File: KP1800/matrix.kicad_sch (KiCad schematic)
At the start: 216 parts

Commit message: Formatted Matrix
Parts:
- removed D103, D104, D105, D106, D107, D108, D18, D36, D72, D90: Diode, symbol ScottoKeebs:Placeholder_Diode
- removed S103, S104, S105, S106, S107, S108, S18, S36, S72, S90: Keyswitch, symbol ScottoKeebs:Placeholder_Keyswitch
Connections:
- net A14: now also S54.1
- net A15: now also S35.1, S53.1, S71.1, S89.1
- net B0: now also S19.1, S37.1, S55.1, S73.1, S91.1
- net B1: now also S20.1, S38.1, S56.1, S74.1, S92.1
- net B10: now also S101.1, S29.1, S47.1, S65.1, S83.1
- net B11: now also S102.1, S30.1, S48.1, S66.1, S84.1
- net B12: now also S31.1, S49.1, S67.1, S85.1
- net B13: now also S32.1, S50.1, S68.1, S86.1
- net B14: now also S33.1, S51.1, S69.1, S87.1
- net B15: now also S34.1, S52.1, S70.1, S88.1
- net B2: now also S21.1, S39.1, S57.1, S75.1, S93.1
- net B3: now also S22.1, S40.1, S58.1, S76.1, S94.1
- net B4: now also S23.1, S41.1, S59.1, S77.1, S95.1
- net B5: now also S24.1, S42.1, S60.1, S78.1, S96.1
- net B6: now also S25.1, S43.1, S61.1, S79.1, S97.1
- net B7: now also S26.1, S44.1, S62.1, S80.1, S98.1
- net B8: now also S27.1, S45.1, S63.1, S81.1, S99.1
- net B9: now also S100.1, S28.1, S46.1, S64.1, S82.1
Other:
- title: (none) -> KP1800 Matrix
- moved on the sheet: D1, D10, D100, D101, D102, D11, D12, D13, D14, D15, D16, D17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

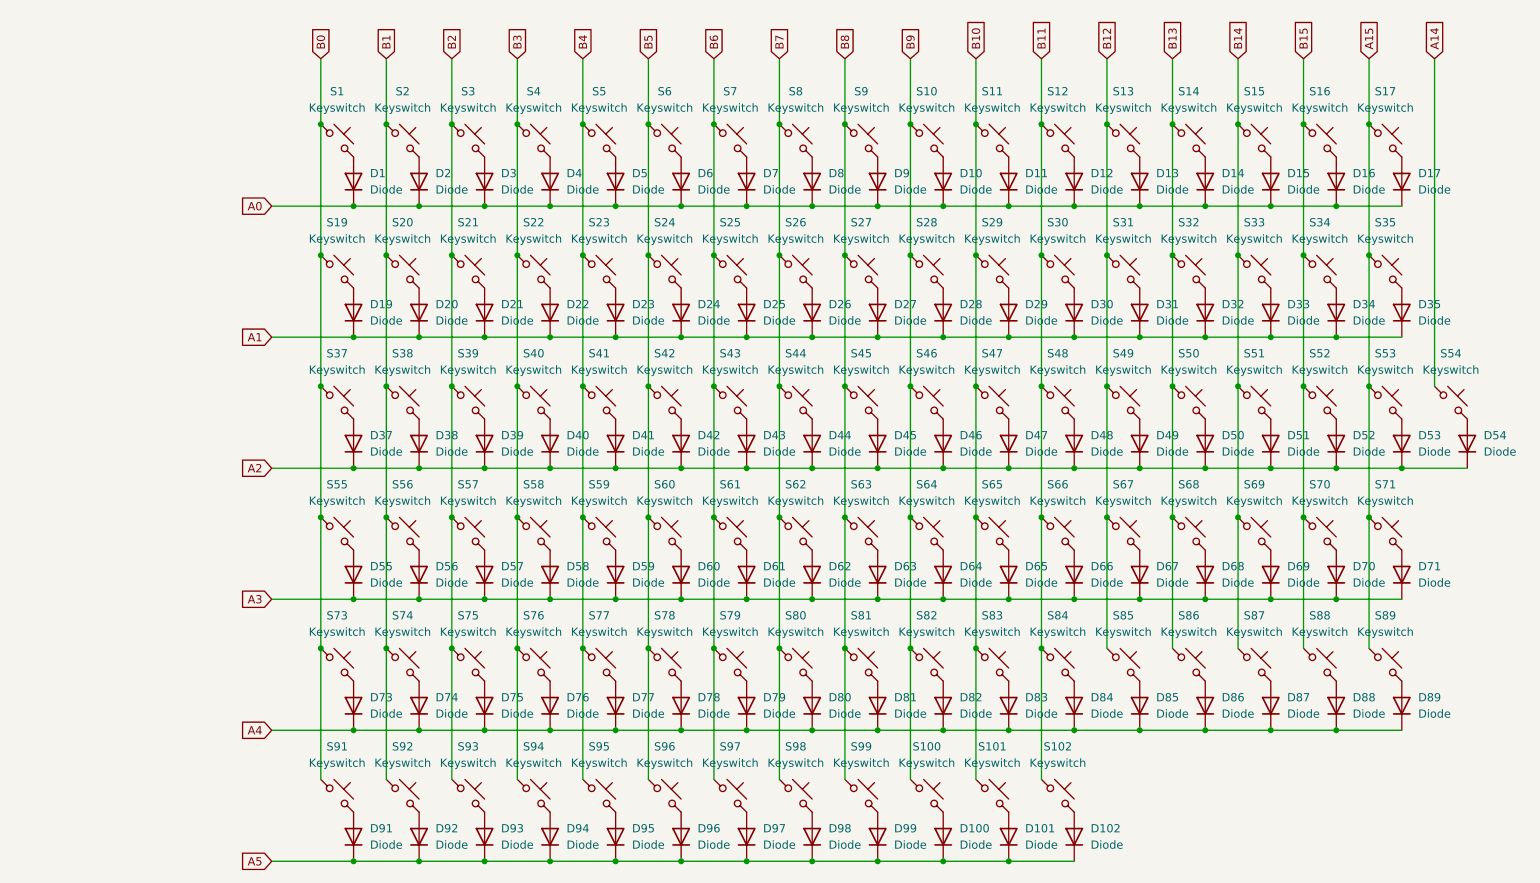
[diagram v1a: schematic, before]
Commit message: Working on PCB // Laid out key switches // 60% board
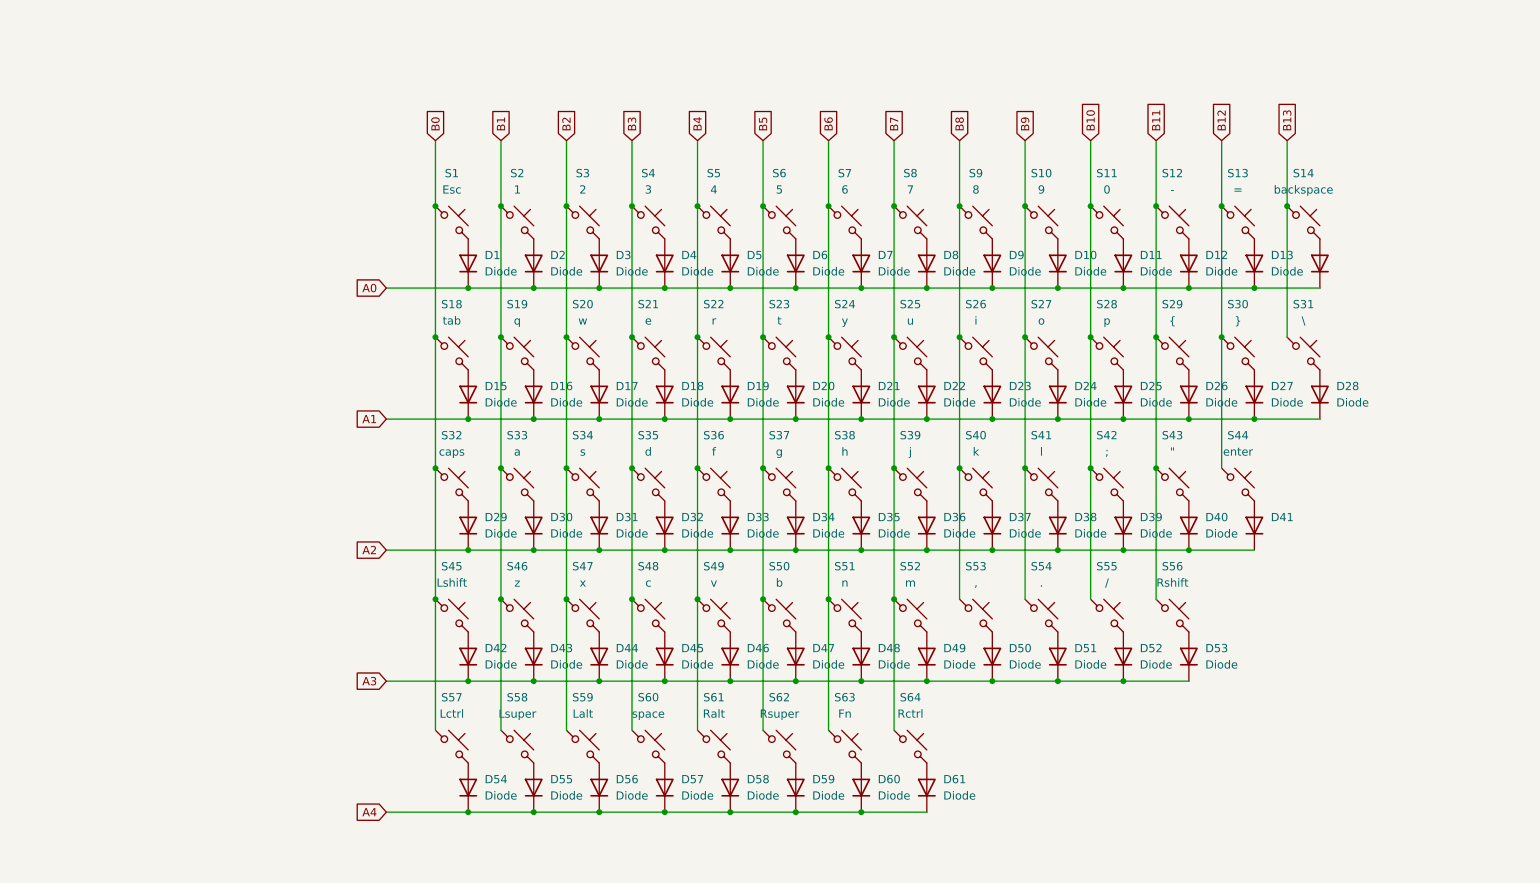
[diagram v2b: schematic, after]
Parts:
- removed D100, D101, D102, D62, D63, D64, D65, D66, D67, D68, D69, D70, D71, D73, D74, D75, D76, D77, D78, D79, D80, D81, D82, D83, D84, D85, D86, D87, D88, D89, D91, D92, D93, D94, D95, D96, D97, D98, D99: Diode, symbol ScottoKeebs:Placeholder_Diode
- removed S100, S101, S102, S15, S16, S17, S65, S66, S67, S68, S69, S70, S71, S73, S74, S75, S76, S77, S78, S79, S80, S81, S82, S83, S84, S85, S86, S87, S88, S89, S91, S92, S93, S94, S95, S96, S97, S98, S99: Keyswitch, symbol ScottoKeebs:Placeholder_Keyswitch
- added D18, D36: Diode, Diode_SMD:D_SOD-123, symbol ScottoKeebs:Placeholder_Diode
- added S18: tab, ScottoKeebs_MX:MX_PCB_1.50u, symbol ScottoKeebs:Placeholder_Keyswitch
- added S36: f, ScottoKeebs_MX:MX_PCB_1.00u, symbol ScottoKeebs:Placeholder_Keyswitch
- D1, D10, D11, D12, D13, D14, D15, D16, D17, D19, D2, D20, D21, D22, D23, D24, D25, D26, D27, D28, D29, D3, D30, D31, D32, D33, D34, D35, D37, D38, D39, D4, D40, D41, D42, D43, D44, D45, D46, D47, D48, D49, D5, D50, D51, D52, D53, D54, D55, D56, D57, D58, D59, D6, D60, D61, D7, D8, D9: footprint (none) -> Diode_SMD:D_SOD-123
- S1: value Keyswitch -> Esc; footprint (none) -> ScottoKeebs_MX:MX_PCB_1.00u
- S10: value Keyswitch -> 9; footprint (none) -> ScottoKeebs_MX:MX_PCB_1.00u
- S11: value Keyswitch -> 0; footprint (none) -> ScottoKeebs_MX:MX_PCB_1.00u
- S12: value Keyswitch -> -; footprint (none) -> ScottoKeebs_MX:MX_PCB_1.00u
- S13: value Keyswitch -> =; footprint (none) -> ScottoKeebs_MX:MX_PCB_1.00u
- S14: value Keyswitch -> backspace; footprint (none) -> ScottoKeebs_MX:MX_PCB_2.00u
- S19: value Keyswitch -> q; footprint (none) -> ScottoKeebs_MX:MX_PCB_1.00u
- S2: value Keyswitch -> 1; footprint (none) -> ScottoKeebs_MX:MX_PCB_1.00u
- S20: value Keyswitch -> w; footprint (none) -> ScottoKeebs_MX:MX_PCB_1.00u
- S21: value Keyswitch -> e; footprint (none) -> ScottoKeebs_MX:MX_PCB_1.00u
- S22: value Keyswitch -> r; footprint (none) -> ScottoKeebs_MX:MX_PCB_1.00u
- S23: value Keyswitch -> t; footprint (none) -> ScottoKeebs_MX:MX_PCB_1.00u
- S24: value Keyswitch -> y; footprint (none) -> ScottoKeebs_MX:MX_PCB_1.00u
- S25: value Keyswitch -> u; footprint (none) -> ScottoKeebs_MX:MX_PCB_1.00u
- S26: value Keyswitch -> i; footprint (none) -> ScottoKeebs_MX:MX_PCB_1.00u
- S27: value Keyswitch -> o; footprint (none) -> ScottoKeebs_MX:MX_PCB_1.00u
- S28: value Keyswitch -> p; footprint (none) -> ScottoKeebs_MX:MX_PCB_1.00u
- S29: value Keyswitch -> {; footprint (none) -> ScottoKeebs_MX:MX_PCB_1.00u
- S3: value Keyswitch -> 2; footprint (none) -> ScottoKeebs_MX:MX_PCB_1.00u
- S30: value Keyswitch -> }; footprint (none) -> ScottoKeebs_MX:MX_PCB_1.00u
- S31: value Keyswitch -> \; footprint (none) -> ScottoKeebs_MX:MX_PCB_1.50u
- S32: value Keyswitch -> caps; footprint (none) -> ScottoKeebs_MX:MX_PCB_1.75u
- S33: value Keyswitch -> a; footprint (none) -> ScottoKeebs_MX:MX_PCB_1.00u
- S34: value Keyswitch -> s; footprint (none) -> ScottoKeebs_MX:MX_PCB_1.00u
- S35: value Keyswitch -> d; footprint (none) -> ScottoKeebs_MX:MX_PCB_1.00u
- S37: value Keyswitch -> g; footprint (none) -> ScottoKeebs_MX:MX_PCB_1.00u
- S38: value Keyswitch -> h; footprint (none) -> ScottoKeebs_MX:MX_PCB_1.00u
- S39: value Keyswitch -> j; footprint (none) -> ScottoKeebs_MX:MX_PCB_1.00u
- S4: value Keyswitch -> 3; footprint (none) -> ScottoKeebs_MX:MX_PCB_1.00u
- S40: value Keyswitch -> k; footprint (none) -> ScottoKeebs_MX:MX_PCB_1.00u
- S41: value Keyswitch -> l; footprint (none) -> ScottoKeebs_MX:MX_PCB_1.00u
- S42: value Keyswitch -> ;; footprint (none) -> ScottoKeebs_MX:MX_PCB_1.00u
- S43: value Keyswitch -> "; footprint (none) -> ScottoKeebs_MX:MX_PCB_1.00u
- S44: value Keyswitch -> enter; footprint (none) -> ScottoKeebs_MX:MX_PCB_2.25u
- S45: value Keyswitch -> Lshift; footprint (none) -> ScottoKeebs_MX:MX_PCB_2.25u
- S46: value Keyswitch -> z; footprint (none) -> ScottoKeebs_MX:MX_PCB_1.00u
- S47: value Keyswitch -> x; footprint (none) -> ScottoKeebs_MX:MX_PCB_1.00u
- S48: value Keyswitch -> c; footprint (none) -> ScottoKeebs_MX:MX_PCB_1.00u
- S49: value Keyswitch -> v; footprint (none) -> ScottoKeebs_MX:MX_PCB_1.00u
- S5: value Keyswitch -> 4; footprint (none) -> ScottoKeebs_MX:MX_PCB_1.00u
- S50: value Keyswitch -> b; footprint (none) -> ScottoKeebs_MX:MX_PCB_1.00u
- S51: value Keyswitch -> n; footprint (none) -> ScottoKeebs_MX:MX_PCB_1.00u
- S52: value Keyswitch -> m; footprint (none) -> ScottoKeebs_MX:MX_PCB_1.00u
- S53: value Keyswitch -> ,; footprint (none) -> ScottoKeebs_MX:MX_PCB_1.00u
- S54: value Keyswitch -> .; footprint (none) -> ScottoKeebs_MX:MX_PCB_1.00u
- S55: value Keyswitch -> /; footprint (none) -> ScottoKeebs_MX:MX_PCB_1.00u
- S56: value Keyswitch -> Rshift; footprint (none) -> ScottoKeebs_MX:MX_PCB_2.75u
- S57: value Keyswitch -> Lctrl; footprint (none) -> ScottoKeebs_MX:MX_PCB_1.25u
- S58: value Keyswitch -> Lsuper; footprint (none) -> ScottoKeebs_MX:MX_PCB_1.25u
- S59: value Keyswitch -> Lalt; footprint (none) -> ScottoKeebs_MX:MX_PCB_1.25u
- S6: value Keyswitch -> 5; footprint (none) -> ScottoKeebs_MX:MX_PCB_1.00u
- S60: value Keyswitch -> space; footprint (none) -> ScottoKeebs_MX:MX_PCB_6.25u
- S61: value Keyswitch -> Ralt; footprint (none) -> ScottoKeebs_MX:MX_PCB_1.25u
- S62: value Keyswitch -> Rsuper; footprint (none) -> ScottoKeebs_MX:MX_PCB_1.25u
- S63: value Keyswitch -> Fn; footprint (none) -> ScottoKeebs_MX:MX_PCB_1.25u
- S64: value Keyswitch -> Rctrl; footprint (none) -> ScottoKeebs_MX:MX_PCB_1.25u
- S7: value Keyswitch -> 6; footprint (none) -> ScottoKeebs_MX:MX_PCB_1.00u
- S8: value Keyswitch -> 7; footprint (none) -> ScottoKeebs_MX:MX_PCB_1.00u
- S9: value Keyswitch -> 8; footprint (none) -> ScottoKeebs_MX:MX_PCB_1.00u
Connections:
- net A14 is gone; now on net B9: S54.1
- net A0: no longer D15.1 (K), D16.1 (K), D17.1 (K)
- net A1: now also D15.1 (K), D16.1 (K), D17.1 (K), D18.1 (K); no longer D29.1 (K), D30.1 (K), D31.1 (K), D32.1 (K), D33.1 (K), D34.1 (K), D35.1 (K)
- net A2: now also D29.1 (K), D30.1 (K), D31.1 (K), D32.1 (K), D33.1 (K), D34.1 (K), D35.1 (K), D36.1 (K); no longer D42.1 (K), D43.1 (K), D44.1 (K), D45.1 (K), D46.1 (K), D47.1 (K), D48.1 (K), D49.1 (K), D50.1 (K), D51.1 (K), D52.1 (K), D53.1 (K), D54.1 (K)
- net A3: now also D42.1 (K), D43.1 (K), D44.1 (K), D45.1 (K), D46.1 (K), D47.1 (K), D48.1 (K), D49.1 (K), D50.1 (K), D51.1 (K), D52.1 (K), D53.1 (K); no longer D55.1 (K), D56.1 (K), D57.1 (K), D58.1 (K), D59.1 (K), D60.1 (K), D61.1 (K)
- net A4: now also D54.1 (K), D55.1 (K), D56.1 (K), D57.1 (K), D58.1 (K), D59.1 (K), D60.1 (K), D61.1 (K)
- net B0: now also S32.1, S45.1, S57.1, S18.1; no longer S19.1, S37.1, S55.1
- net B1: now also S19.1, S33.1, S46.1, S58.1; no longer S20.1, S38.1, S56.1
- net B10: now also S28.1, S42.1, S55.1; no longer S29.1, S47.1
- net B11: now also S29.1, S43.1, S56.1; no longer S30.1, S48.1
- net B12: now also S30.1, S44.1; no longer S31.1, S49.1
- net B13: now also S31.1; no longer S32.1, S50.1
- net B2: now also S20.1, S34.1, S47.1, S59.1; no longer S21.1, S39.1, S57.1
- net B3: now also S21.1, S35.1, S48.1, S60.1; no longer S22.1, S40.1, S58.1
- net B4: now also S22.1, S49.1, S61.1, S36.1; no longer S23.1, S41.1, S59.1
- net B5: now also S23.1, S37.1, S50.1, S62.1; no longer S24.1, S42.1, S60.1
- net B6: now also S24.1, S38.1, S51.1, S63.1; no longer S25.1, S43.1, S61.1
- net B7: now also S25.1, S39.1, S52.1, S64.1; no longer S26.1, S44.1, S62.1
- net B8: now also S26.1, S40.1, S53.1; no longer S27.1, S45.1, S63.1
- net B9: now also S27.1, S41.1; no longer S28.1, S46.1, S64.1
- net at S30.2: now also D27.2 (A); no longer D30.2 (A)
- net at S64.2: now also D61.2 (A)
- net at S50.2: now also D47.2 (A); no longer D50.2 (A)
- net at S58.2: now also D55.2 (A); no longer D58.2 (A)
- net at S44.2: now also D41.2 (A); no longer D44.2 (A)
- net at D28.2 (A): now also S31.2; no longer S28.2
- net at S51.2: now also D48.2 (A); no longer D51.2 (A)
- net at D59.2 (A): now also S62.2; no longer S59.2
- net at D60.2 (A): now also S63.2; no longer S60.2
- net at D19.2 (A): now also S22.2; no longer S19.2
- net at D37.2 (A): now also S40.2; no longer S37.2
- net at D31.2 (A): now also S34.2; no longer S31.2
- net at S52.2: now also D49.2 (A); no longer D52.2 (A)
- net at S55.2: now also D52.2 (A); no longer D55.2 (A)
- net at S61.2: now also D58.2 (A); no longer D61.2 (A)
- net at D35.2 (A): now also S38.2; no longer S35.2
- net at D21.2 (A): now also S24.2; no longer S21.2
- net at D23.2 (A): now also S26.2; no longer S23.2
- net at D26.2 (A): now also S29.2; no longer S26.2
- net at D38.2 (A): now also S41.2; no longer S38.2
- net at D17.2 (A): now also S20.2
- net at S57.2: now also D54.2 (A); no longer D57.2 (A)
- net at D20.2 (A): now also S23.2; no longer S20.2
- net at D34.2 (A): now also S37.2; no longer S34.2
- net at S56.2: now also D53.2 (A); no longer D56.2 (A)
- net at D29.2 (A): now also S32.2; no longer S29.2
- net at S47.2: now also D44.2 (A); no longer D47.2 (A)
- net at S27.2: now also D24.2 (A); no longer D27.2 (A)
- net at D16.2 (A): now also S19.2
- net at D45.2 (A): now also S48.2; no longer S45.2
- net at D40.2 (A): now also S43.2; no longer S40.2
- net at S49.2: now also D46.2 (A); no longer D49.2 (A)
- net at D22.2 (A): now also S25.2; no longer S22.2
- net at D43.2 (A): now also S46.2; no longer S43.2
- net at D32.2 (A): now also S35.2; no longer S32.2
- net at D39.2 (A): now also S42.2; no longer S39.2
- net at S54.2: now also D51.2 (A); no longer D54.2 (A)
- net at D25.2 (A): now also S28.2; no longer S25.2
- net at S53.2: now also D50.2 (A); no longer D53.2 (A)
- net at D15.2 (A): now also S18.2
- net at D42.2 (A): now also S45.2; no longer S42.2
- net at D33.2 (A): now also S36.2; no longer S33.2
- removed net A15: S35.1, S53.1
- removed net B14: S33.1, S51.1
- removed net B15: S34.1, S52.1
- new net: D18.2 (A), S21.2
- new net: D57.2 (A), S60.2
- new net: D56.2 (A), S59.2
- new net: D30.2 (A), S33.2
- new net: D36.2 (A), S39.2
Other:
- moved on the sheet: S1, S10, S11, S12, S13, S14, S2, S3, S4, S5, S6, S7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

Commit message: All traces done. Now working on grounding.
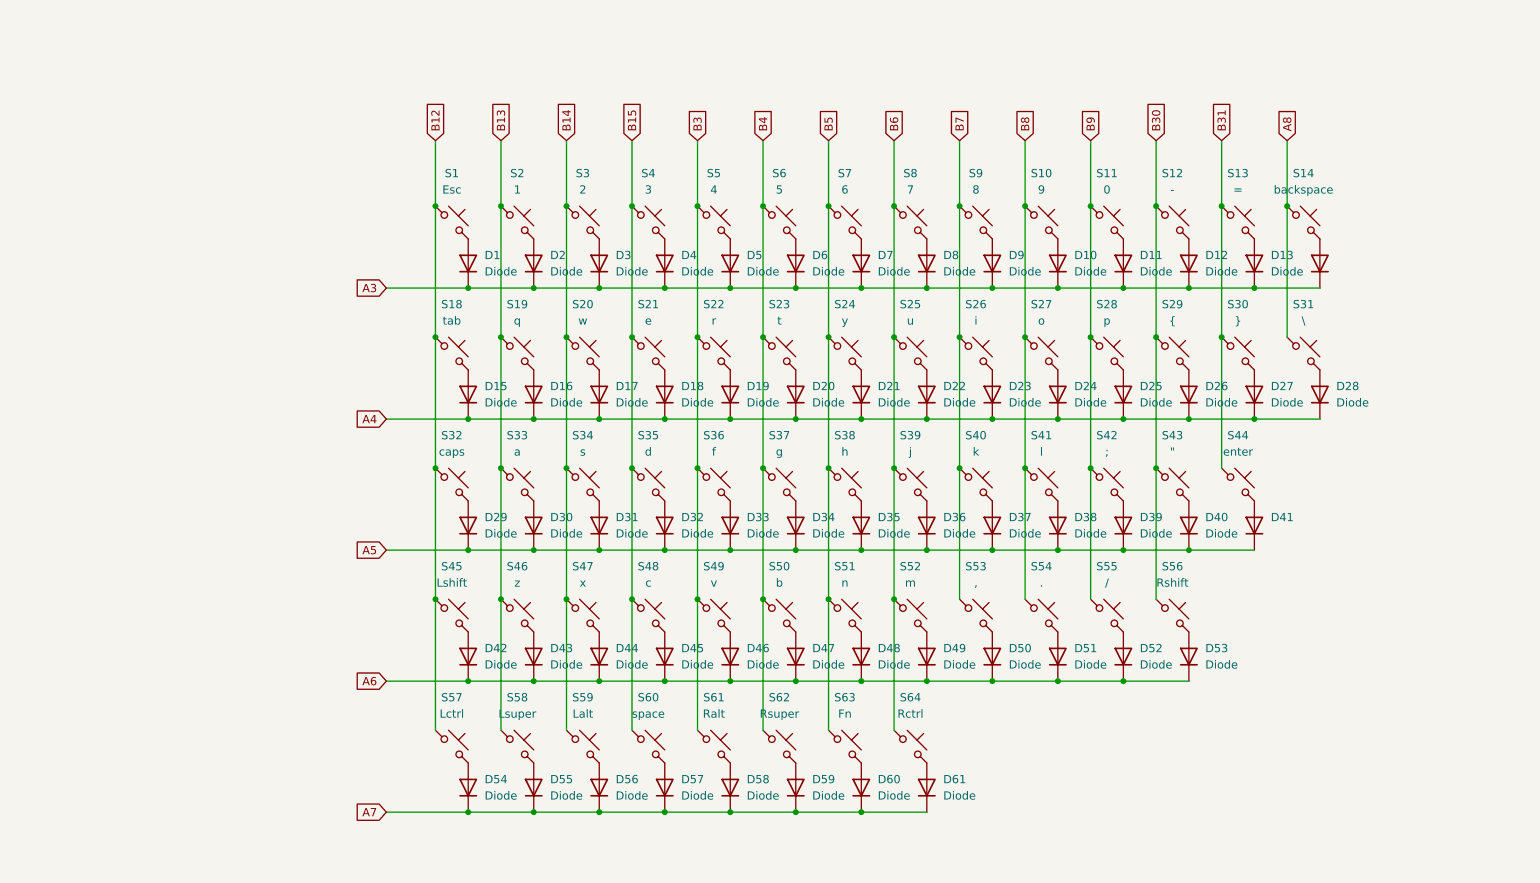
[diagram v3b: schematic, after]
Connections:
- net A0 is gone; now on net A3: D1.1 (K), D10.1 (K), D11.1 (K), D12.1 (K), D13.1 (K), D14.1 (K), D2.1 (K), D3.1 (K), D4.1 (K), D5.1 (K), D6.1 (K), D7.1 (K), D8.1 (K), D9.1 (K)
- net A1 is gone; now on net A4: D15.1 (K), D16.1 (K), D17.1 (K), D18.1 (K), D19.1 (K), D20.1 (K), D21.1 (K), D22.1 (K), D23.1 (K), D24.1 (K), D25.1 (K), D26.1 (K), D27.1 (K), D28.1 (K)
- net B0 is gone; now on net B12: S1.1, S18.1, S32.1, S45.1, S57.1
- net B1 is gone; now on net B13: S19.1, S2.1, S33.1, S46.1, S58.1
- net B10 is gone; now on net B9: S11.1, S28.1, S42.1, S55.1
- net A3: no longer D42.1 (K), D43.1 (K), D44.1 (K), D45.1 (K), D46.1 (K), D47.1 (K), D48.1 (K), D49.1 (K), D50.1 (K), D51.1 (K), D52.1 (K), D53.1 (K)
- net A4: no longer D54.1 (K), D55.1 (K), D56.1 (K), D57.1 (K), D58.1 (K), D59.1 (K), D60.1 (K), D61.1 (K)
- net B12: no longer S13.1, S30.1, S44.1
- net B13: no longer S14.1, S31.1
- net B3: now also S22.1, S36.1, S49.1, S5.1, S61.1; no longer S21.1, S35.1, S4.1, S48.1, S60.1
- net B4: now also S23.1, S37.1, S50.1, S6.1, S62.1; no longer S22.1, S36.1, S49.1, S5.1, S61.1
- net B5: now also S24.1, S38.1, S51.1, S63.1, S7.1; no longer S23.1, S37.1, S50.1, S6.1, S62.1
- net B6: now also S25.1, S39.1, S52.1, S64.1, S8.1; no longer S24.1, S38.1, S51.1, S63.1, S7.1
- net B7: now also S26.1, S40.1, S53.1, S9.1; no longer S25.1, S39.1, S52.1, S64.1, S8.1
- net B8: now also S10.1, S27.1, S41.1, S54.1; no longer S26.1, S40.1, S53.1, S9.1
- net B9: no longer S10.1, S27.1, S41.1, S54.1
- net A2 renamed A5
- net B11 renamed B30
- net B2 renamed B14
- new net A6: D42.1 (K), D43.1 (K), D44.1 (K), D45.1 (K), D46.1 (K), D47.1 (K), D48.1 (K), D49.1 (K), D50.1 (K), D51.1 (K), D52.1 (K), D53.1 (K)
- new net A7: D54.1 (K), D55.1 (K), D56.1 (K), D57.1 (K), D58.1 (K), D59.1 (K), D60.1 (K), D61.1 (K)
- new net A8: S14.1, S31.1
- new net B15: S21.1, S35.1, S4.1, S48.1, S60.1
- new net B31: S13.1, S30.1, S44.1
